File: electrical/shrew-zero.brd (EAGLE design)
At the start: 18 x 20 mm, 44 parts, among them IC1 LMR16006YQ3DDCTQ1, U1 ESP32-PICO-D4, U2 SX1280IMLTRT, X5 PIN-1X-BIG, X6 PIN-1X-BIG, Y1 52MHz TCXO

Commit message: shrew-zero major update
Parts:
- moved JP1 4.50 mm to (12.8, 1.20)
- moved C26 1.99 mm to (10.2, 5.30)
- moved L2 1.99 mm to (12.2, 5.50)
- moved C14 1.99 mm to (13.1, 4.80)
- moved C16 1.99 mm to (5.50, 4.80)
- moved C18 1.99 mm to (3.60, 4.80)
- moved C19 1.99 mm to (3.50, 4.80)
- moved C20 1.99 mm to (5.50, 4.80)
- moved D2 1.99 mm to (12.5, 3.80)
- moved IC1 1.99 mm to (8.10, 4.50)
- moved C21 1.98 mm to (7.40, 4.80)
- moved C23 1.98 mm to (11.2, 4.80)
- moved C22 1.98 mm to (9.30, 4.80)
- moved R4 1.21 mm to (15.3, 6.30), turned to 180 degrees
- moved C25 0.40 mm to (16.1, 4.90)
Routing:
- net 3.3V: track 38.4 -> 49.0 mm
- net SIG4: track 7.55 -> 12.3 mm, vias 0 -> 2
- net SIG3: track 6.01 -> 10.6 mm, vias 0 -> 1
- net SIG2: track 14.7 -> 19.2 mm, vias 2 -> 3
- net SIG1: track 12.6 -> 16.7 mm, vias 2 -> 3
- net GND: track 38.1 -> 36.4 mm, vias 27 -> 31
- net V-ADC: track 3.02 -> 1.89 mm
- net +24V: track 23.6 -> 24.2 mm, vias 0 -> 1
- added copper zone on layer 15, net GND

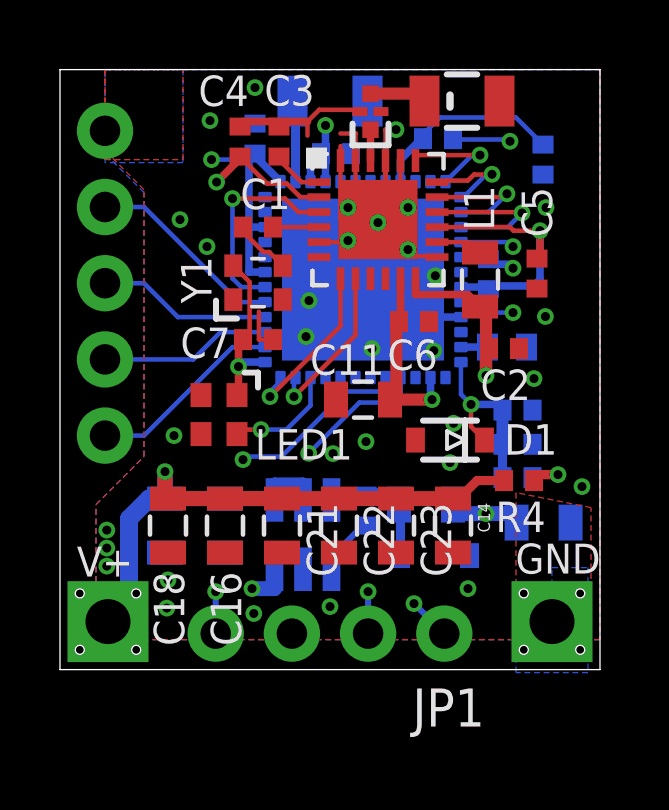
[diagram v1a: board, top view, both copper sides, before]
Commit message: sorted component ref des
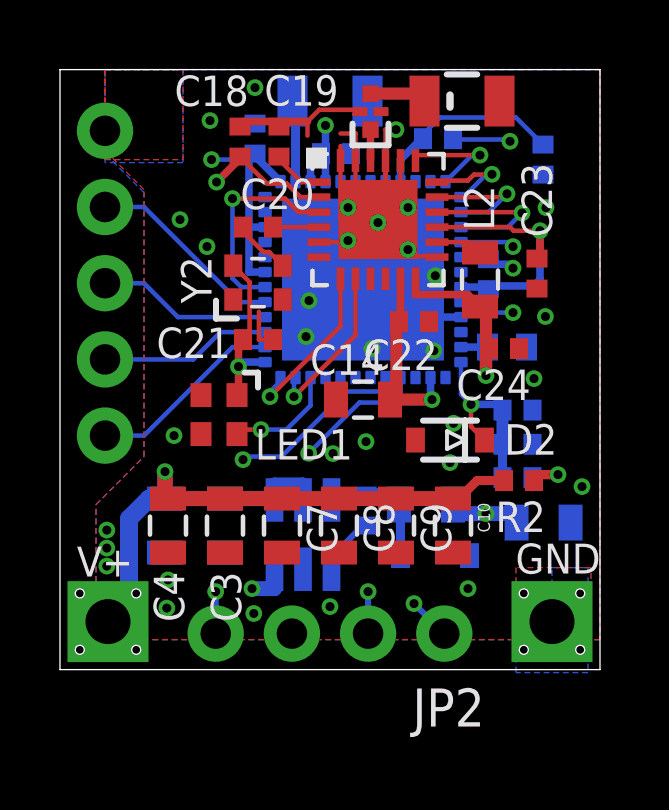
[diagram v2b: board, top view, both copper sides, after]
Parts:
- removed C25: 10u, shrew-common:0805
- removed C26: 100n, shrew-common:0402-REV
- removed EDGE1: (no value), shrew-common:1X05
- removed FL1: 2450FM07D0034T, shrew-core:FIL_2450FM07D0034T
- added C15, C24: 470n, shrew-common:0402-REV
- added JP2: (no value), shrew-common:1X04-CLEAN
- added Y2: 52MHz TCXO, shrew-common:OSC_TG2016SMN_50.0000M-ECGNNMB
- C1: value 1n -> 100n
- C10, C5, C6, C7, C8, C9: value 100n -> 10u; device shrew-common:0402-REV -> shrew-common:0805
- C11: value 10uF 25V -> 100n; device shrew-common:0805 -> shrew-common:0402-REV
- C12: value DNP -> 100n; device shrew-common:0402-CAP -> shrew-common:0402-REV
- C13: value 470n -> 100n
- C14: value 10u -> 10uF 25V
- C16: value 10u -> DNP; device shrew-common:0805 -> shrew-common:0402-CAP
- C18, C19: value 10u -> 10n; device shrew-common:0805 -> shrew-common:0402-REV
- C2: value 470n -> 10u; device shrew-common:0402-REV -> shrew-common:0805
- C20: value 10u -> 1n; device shrew-common:0805 -> shrew-common:0402-REV
- C21, C22, C23: value 10u -> 100n; device shrew-common:0805 -> shrew-common:0402-REV
- C3, C4: value 10n -> 10u; device shrew-common:0402-REV -> shrew-common:0805
- D1: value 3V6 -> (none)
- D2: value (none) -> 3V6
- JP1: device shrew-common:1X04-CLEAN -> shrew-common:1X05
- L1: value 15u -> 6u8
- L2: value 6u8 -> 15u
- R2: value 10K -> 68K
- R4: value 68K -> 10K
- Y1: value 52MHz TCXO -> 2450FM07D0034001T; device shrew-common:OSC_TG2016SMN_50.0000M-ECGNNMB -> shrew-core:FIL_2450FM07D0034T
- moved C5 15.0 mm to (3.50, 4.80), flipped to the bottom, turned to 270 degrees
- moved C10 14.5 mm to (13.1, 4.80), flipped to the top, turned to 270 degrees
- moved C19 13.4 mm to (7.30, 17.6), flipped to the top
- moved JP1 13.1 mm to (1.50, 7.80), turned to 90 degrees
- moved C18 13.0 mm to (6.00, 17.6)
- moved C4 13.0 mm to (3.60, 4.80)
- moved C3 12.9 mm to (5.50, 4.80)
- moved C8 12.4 mm to (9.30, 4.80), flipped to the top, turned to 270 degrees
- moved C16 11.1 mm to (14.9, 10.8), flipped to the bottom, turned to 0 degrees
- moved C1 10.1 mm to (10.2, 5.30), flipped to the bottom, turned to 270 degrees
- moved C20 10.0 mm to (6.60, 14.8), flipped to the top, turned to 0 degrees
- moved C23 9.63 mm to (15.9, 13.2), turned to 90 degrees
- moved C11 9.42 mm to (6.50, 17.7), flipped to the bottom, turned to 90 degrees
- moved C6 9.27 mm to (5.50, 4.80), flipped to the bottom, turned to 270 degrees
- moved C9 8.93 mm to (11.2, 4.80), flipped to the top, turned to 270 degrees
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- renumbered X5 to X1, X6 to X2
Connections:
- net +24V: now also C10.1, C3.1, C4.1, C5.1, C6.1, C7.1, C8.1, C9.1, R2.2; no longer C14.1, C16.1, C18.1, C19.1, C20.1, C21.1, C22.1, C23.1, R4.2
- net 3.3V: now also C12.1, C13.1, C14.1, C2.1, C21.2, C22.2, C23.2, L1.2, Y2.4; no longer C10.1, C25.1, C5.2, C6.2, C7.2, C8.1, C9.1, L2.2, Y1.4
- net AUX1: now also JP1.1; no longer EDGE1.1
- net AUX2: now also JP1.2; no longer EDGE1.2
- net BATT-ADC: now also D2.1, R4.2; no longer D1.1, R2.2
- net ESP-BOOT: now also C16.2; no longer C12.2
- net ESP-EN: now also C15.2; no longer C13.2
- net GND: now also C12.2, C13.2, C15.1, C16.1, C18.1, C19.1, C2.2, C21.1, C22.1, C23.1, C24.1, C3.2, C4.2, C5.2, C6.2, C7.2, JP1.5, R4.1, Y1.4, Y2.2; no longer C12.1, C13.1, C16.2, C18.2, C19.2, C2.1, C20.2, C21.2, C22.2, C23.2, C25.2, C3.1, C4.1, C5.1, C6.1, C7.1, EDGE1.5, FL1.2, FL1.4, R2.1
- net N$10: now also C1.1, D1.1, L1.1; no longer C26.1, D2.1, L2.1
- net N$11: now also C19.2; no longer C3.2
- net N$2: now also C20.1, Y2.3; no longer C1.1, Y1.3
- net N$3: now also C20.2; no longer C1.2
- net N$4: now also C1.2; no longer C26.2
- net N$6: now also Y1.1; no longer FL1.1
- net N$7: now also Y1.3; no longer FL1.3
- net N$9: now also L2.2; no longer L1.2
- net RADIO-VDD: now also C18.2, C24.2, L2.1; no longer C2.2, C4.2, L1.1
- net SIG1: now also JP2.1; no longer JP1.1
- net SIG2: now also JP2.2; no longer JP1.2
- net SIG3: now also JP2.3; no longer JP1.3
- net SIG4: now also JP2.4; no longer JP1.4
- net U0RXD: now also JP1.3; no longer EDGE1.3
- net U0TXD: now also JP1.4; no longer EDGE1.4
- net V-ADC: now also R2.1; no longer R4.1
